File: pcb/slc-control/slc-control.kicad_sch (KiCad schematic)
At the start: 78 parts, among them J1 USB_C_Receptacle_USB2.0_16P, J2 Conn_01x02_Socket, J3 Conn_01x02_Socket, J4 Conn_01x02_Socket, J5 Conn_01x02_Socket, J7 Conn_ARM_SWD_TagConnect_TC203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, J8 Conn_01x07_Pin, Q3 AO3400A, Q4 AO3401A, Q5 AO3400A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

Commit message: Final pcb
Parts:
- removed AE1: Antenna_Shield, symbol Device:Antenna_Shield
- added C32, C35: 2u2, Capacitor_SMD:C_0402_1005Metric, symbol Device:C
- added C33, C34: 100n, Capacitor_SMD:C_0402_1005Metric, symbol Device:C
- added J6: Conn_Coaxial, User_Footprints:BWSMA-KWE-Z001, symbol Connector:Conn_Coaxial
- added U9: ICM-42688-P, Package_LGA:LGA-14_3x2.5mm_P0.5mm_LayoutBorder3x4y, symbol User_Symbols:ICM-42688-P
- U7: LCSC (none) -> C529355
- U8: footprint RF_GPS:Quectel_L70-R -> User_Footprints:GPS02-UBX
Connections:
- net +3V3: now also C32.1, C33.1, C34.1, C35.1, U9.5 (VDDIO), U9.8 (VDD)
- net ANT: now also J6.1 (In)
- net GND: now also C32.2, C33.2, C34.2, C35.2, J6.2 (Ext), U9.11 (RESV), U9.6 (GND), U9.7 (RESV)
- net MISO: now also U9.1 (SDO)
- net MOSI: now also U9.14 (SDI)
- net SCK: now also U9.13 (CLK)
- net SNS1: now also J4.2 (Pin_2); no longer J4.1 (Pin_1)
- net SNS2: now also J4.1 (Pin_1); no longer J4.2 (Pin_2)
- net SNS3: now also J5.2 (Pin_2); no longer J5.1 (Pin_1)
- net SWCLK: now also U7.38 (PA14)
- net SWDIO: now also U7.37 (PA13)
- net SWO: now also U7.40 (PB3)
- net USB+: now also U7.34 (PA12)
- net USB-: now also U7.33 (PA11)
- net at JP1.2 (C): now also J5.1 (Pin_1); no longer J5.2 (Pin_2)
- new net CSG: U9.12 (CS)
- new net INTG1: U9.4 (INT1)
- new net INTG2: U9.9 (INT2)
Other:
- note added: "IMU"
- note removed: "CHOOSE SMA CONNECTOR"
- note removed: "POSSIBLY ADD GYRO"
- moved on the sheet: BT1, C10, C14, C15, C21, C28, C29, C30, C31, C5, C7, D5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

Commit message: Finish layout
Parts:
- removed JP1: SolderJumper_3_Open, Jumper:SolderJumper-3_P1.3mm_Open_RoundedPad1.0x1.5mm, symbol Jumper:SolderJumper_3_Open
- removed R11: 10k, Resistor_SMD:R_0402_1005Metric, symbol Device:R
- added C36: 100n, Capacitor_SMD:C_0402_1005Metric, symbol Device:C
- added R3: 33k, Resistor_SMD:R_0402_1005Metric, symbol Device:R
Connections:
- net BOOT0 is gone; now on net BTN4: U7.45 (PB8)
- net GRST is gone; now on net +3V3: U8.18 (~{RST})
- net +3V3: no longer U7.20 (VREF+)
- net +5V: now also R3.1
- net BTN1: now also U7.4 (PC15)
- net BTN2: now also U7.3 (PC14)
- net BTN3: now also U7.2 (PC13)
- net CSD: now also U7.28 (PB14)
- net CSG: now also U7.12 (PA4)
- net CSP: now also U7.10 (PA2)
- net DC: now also U7.26 (PB12)
- net DRDYM: now also U7.32 (PA10)
- net DRDYP: now also U7.18 (PB2)
- net DRV1: now also U7.41 (PB4)
- net DRV2: now also U7.42 (PB5)
- net GND: now also C36.2
- net GRX: now also U7.25 (PB11)
- net GTX: now also U7.22 (PB10)
- net INTG1: now also U7.16 (PB0)
- net MISO: now also U7.14 (PA6)
- net MOSI: now also U7.15 (PA7); no longer J8.4 (Pin_4)
- net PPS: now also U7.17 (PB1)
- net REP: now also J5.1 (Pin_1)
- net REPH: now also U7.43 (PB6)
- net REPL: now also U7.46 (PB9)
- net RES: now also C23.1, R3.2
- net RST: now also C36.1; no longer C23.1
- net SCK: now also U7.13 (PA5); no longer J8.3 (Pin_3)
- net SCLE: now also U7.39 (PA15)
- net SCLM: now also U7.31 (PA9)
- net SDAE: now also U7.44 (PB7)
- net SDAM: now also U7.30 (PA8)
- net SIG1: now also U7.11 (PA3)
- net SIG2: now also U7.9 (PA1)
- net SIG3: now also U7.8 (PA0)
- net XTALI: now also C18.2, Y1.1; no longer R10.2
- net XTALO: now also R10.2; no longer C18.2, Y1.1
- net SDK: now reaches U7.27 (PB13)
- net SDK: now also J8.3 (Pin_3)
- net SDI: now reaches U7.29 (PB15)
- net SDI: now also J8.4 (Pin_4)
- net +3VA3 renamed +3V3A
- net +3V3A: now also U7.20 (VREF+)
- net INTG2: no longer names the net of U9.9 (INT2)
- no-connect marks 8 -> 9
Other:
- moved on the sheet: C16, C17, C18, C19, C20, C22, C24, J7, R10, Y1

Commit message: Change extended parts to do not place
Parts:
- BT1, J2, J3, J4, J5, J6, SW1, SW2, SW3, SW4, U8: now not fitted
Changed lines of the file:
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@@
 		(in_bom yes)
 		(on_board yes)
-		(dnp no)
+		(dnp yes)
 		(fields_autoplaced yes)
 		(property "Reference" "J3"
@@
 		(in_bom yes)
 		(on_board yes)
-		(dnp no)
+		(dnp yes)
 		(property "Reference" "J4"
 			(at 52.07 175.2601 0)
@@
 		(in_bom yes)
 		(on_board yes)
-		(dnp no)
+		(dnp yes)
 		(property "Reference" "J6"
 			(at 330.2 41.402 0)
@@
 		(in_bom yes)
 		(on_board yes)
-		(dnp no)
+		(dnp yes)
 		(property "Reference" "J5"
 			(at 52.07 182.8801 0)
@@
 		(in_bom yes)
 		(on_board yes)
-		(dnp no)
+		(dnp yes)
 		(property "Reference" "BT1"
 			(at 268.732 46.736 0)
@@
 		(in_bom yes)
 		(on_board yes)
-		(dnp no)
+		(dnp yes)
 		(fields_autoplaced yes)
 		(property "Reference" "SW2"
@@
 		(in_bom yes)
 		(on_board yes)
-		(dnp no)
+		(dnp yes)
 		(fields_autoplaced yes)
 		(property "Reference" "SW4"
@@
 		(in_bom yes)
 		(on_board yes)
-		(dnp no)
+		(dnp yes)
 		(fields_autoplaced yes)
 		(property "Reference" "SW1"
@@
 		(in_bom yes)
 		(on_board yes)
-		(dnp no)
+		(dnp yes)
 		(property "Reference" "U8"
 			(at 282.956 70.358 0)
@@
 		(in_bom yes)
 		(on_board yes)
-		(dnp no)
+		(dnp yes)
 		(fields_autoplaced yes)
 		(property "Reference" "J2"
@@
 		(in_bom yes)
 		(on_board yes)
-		(dnp no)
+		(dnp yes)
 		(fields_autoplaced yes)
 		(property "Reference" "SW3"

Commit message: Final production
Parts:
- L2: now not fitted
- R9: LCSC (none) -> C25900
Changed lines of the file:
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@@
+			)
+		)
+		(property "LCSC" "C25900"
+			(at 243.84 247.65 0)
+			(effects
+				(font
+					(size 1.27 1.27)
+				)
+				(hide yes)
 			)
 		)
@@
 		(in_bom yes)
 		(on_board yes)
-		(dnp no)
+		(dnp yes)
 		(fields_autoplaced yes)
 		(property "Reference" "L2"

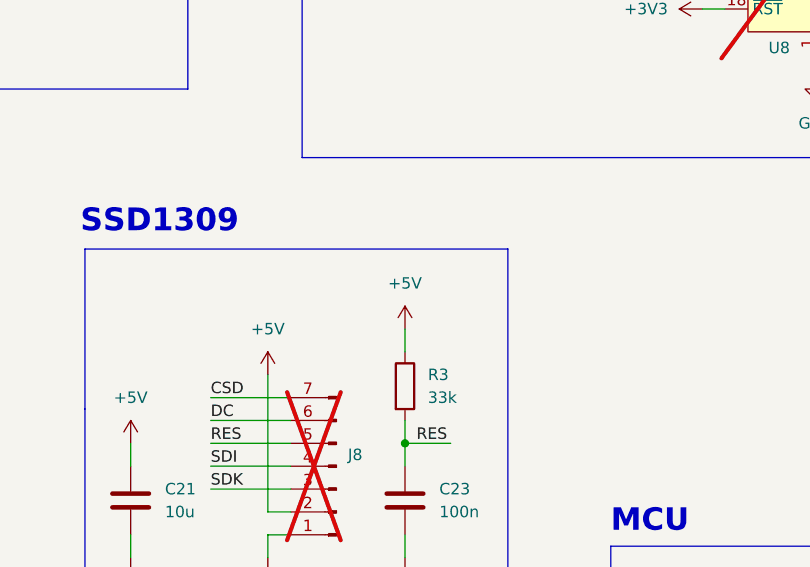
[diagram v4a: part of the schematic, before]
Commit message: Fix ssd1309 reset input voltage
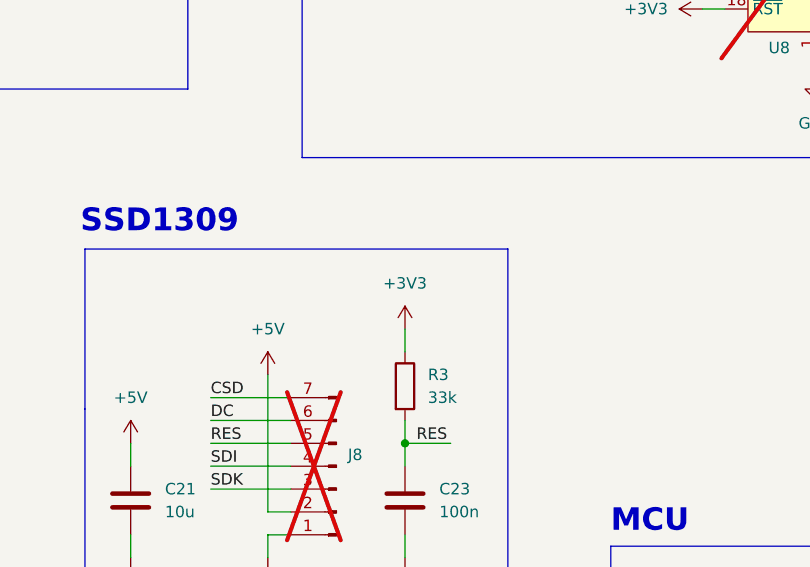
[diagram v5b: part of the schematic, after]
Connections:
- net +3V3: now also R3.1
- net +5V: no longer R3.1

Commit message: Save
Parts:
- U4: LCSC (none) -> C976032
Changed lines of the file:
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@@
+			)
+		)
+		(property "LCSC" "C976032"
+			(at 107.95 43.18 0)
+			(effects
+				(font
+					(size 1.27 1.27)
+				)
+				(hide yes)
 			)
 		)
